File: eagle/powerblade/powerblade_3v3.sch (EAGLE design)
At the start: 78 parts, among them J1 JTAG_14PIN_IDC-ND, J2 AC_INF45, J4 TC2030-JLINK-NL, Q1 NTS4173, Q4 2SK1829, U1 TPS62122, U2 MCP6V3, U3 MSP430FR5738, U4 NRF51822QF, U6 MAX9910, U7 OPA2369, X1 16MHz, X3 32.768kHz, Y1 UREACH_XTEND

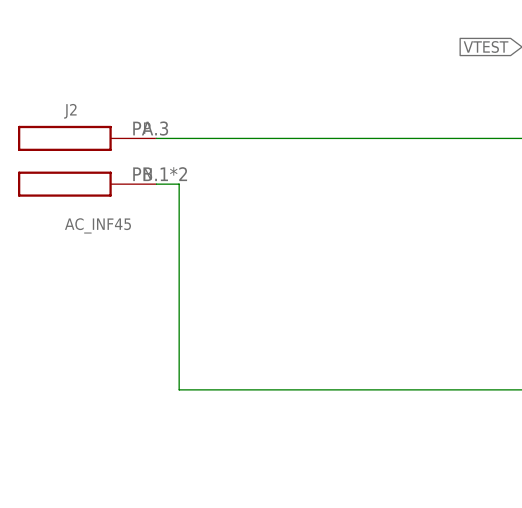
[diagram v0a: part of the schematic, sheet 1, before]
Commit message: added final v5 part (package) and inputted into powerblade
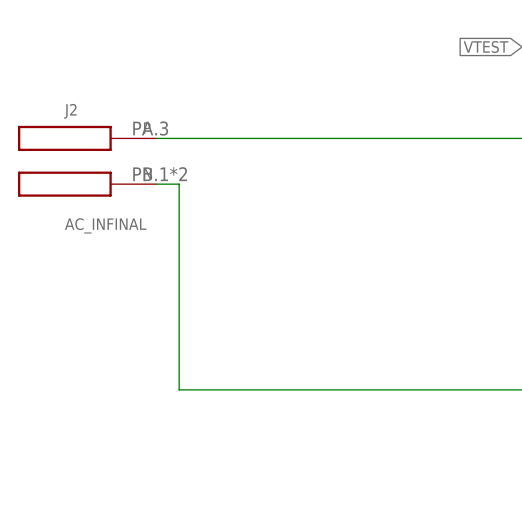
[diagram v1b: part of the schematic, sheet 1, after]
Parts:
- J2: value AC_INF45 -> AC_INFINAL; device powerfilm:AC_INF45 -> powerfilm:AC_INFINAL
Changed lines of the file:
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@@
 <?xml version="1.0" encoding="utf-8"?>
 <!DOCTYPE eagle SYSTEM "eagle.dtd">
-<eagle version="6.5.0">
+<eagle version="6.3">
 <drawing>
 <settings>
@@
 <attribute name="DIGIKEY" value="490-4025-1-ND"/>
 </part>
-<part name="J2" library="powerfilm" deviceset="AC_IN" device="F45" value="AC_INF45">
+<part name="J2" library="powerfilm" deviceset="AC_IN" device="FINAL" value="AC_INFINAL">
 <attribute name="DIGIKEY" value="ED1649-ND"/>
 <attribute name="DIGIKEY_2" value="ED1649-ND"/>
